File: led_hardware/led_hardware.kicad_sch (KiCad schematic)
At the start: 4 parts, among them Q2 BSS138, U1 STM32F303K8T6

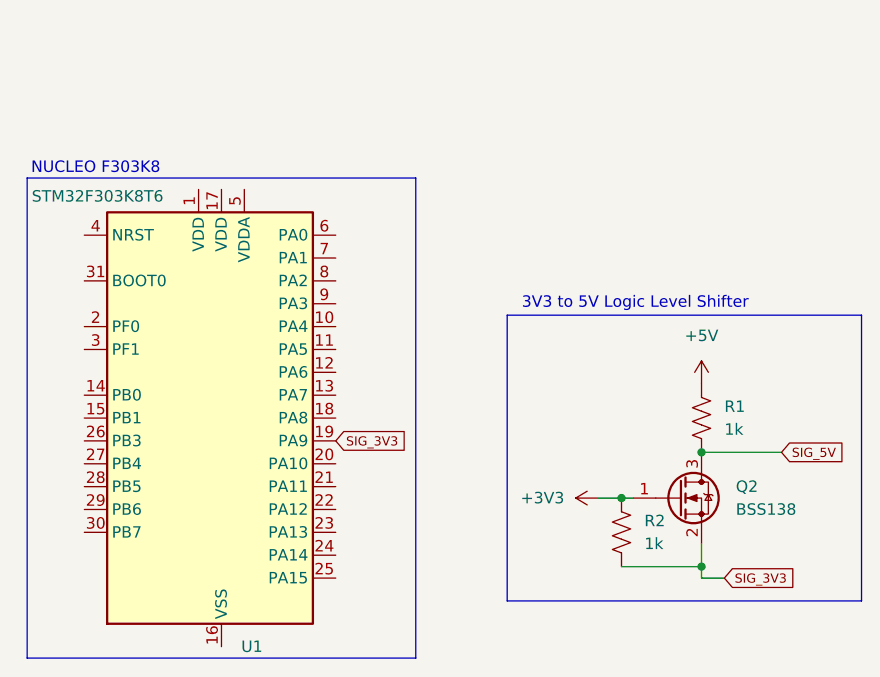
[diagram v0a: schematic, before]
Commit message: used internal timer interrupt to allow for blinking
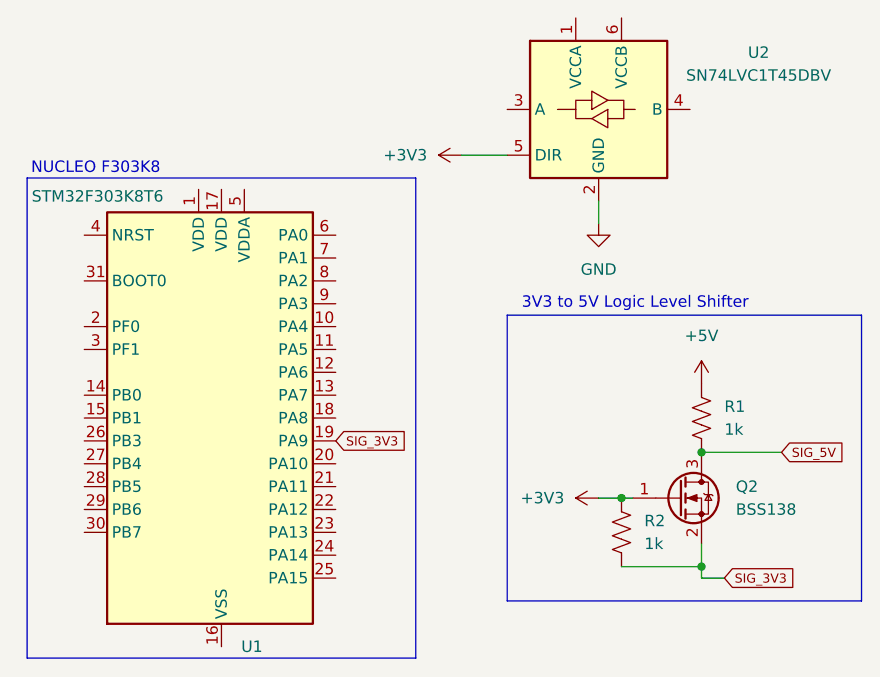
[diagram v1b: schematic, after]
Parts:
- added U2: SN74LVC1T45DBV, Package_TO_SOT_SMD:SOT-23-6, symbol Logic_LevelTranslator:SN74LVC1T45DBV
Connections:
- net +3V3: now also U2.5 (DIR)
- new net GND: U2.2 (GND)
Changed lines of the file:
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@@
+	(wire
+		(pts
+			(xy 151.13 63.5) (xy 151.13 66.04)
+		)
+		(stroke
+			(width 0)
+			(type default)
+		)
+	)
 	(wire
 		(pts
@@
 		(pts
 			(xy 162.56 101.6) (xy 162.56 104.14)
+		)
+		(stroke
+			(width 0)
+			(type default)
+		)
+	)
+	(wire
+		(pts
+			(xy 135.89 58.42) (xy 140.97 58.42)
 		)
 		(stroke
@@
 	)
 	(symbol
+		(lib_id "power:+3V3")
+		(at 135.89 58.42 90)
+		(unit 1)
+		(exclude_from_sim no)
+		(in_bom yes)
+		(on_board yes)
+		(dnp no)
+		(fields_autoplaced yes)
+		(property "Reference" "#PWR03"
+			(at 139.7 58.42 0)
+			(effects
+				(font
+					(size 1.27 1.27)
+				)
+				(hide yes)
+			)
+		)
+		(property "Value" "+3V3"
+			(at 132.08 58.4199 90)
+			(effects
+				(font
+					(size 1.27 1.27)
+				)
+				(justify left)
+			)
+		)
+		(property "Footprint" ""
+			(at 135.89 58.42 0)
+			(effects
+				(font
+					(size 1.27 1.27)
+				)
+				(hide yes)
+			)
+		)
+		(property "Datasheet" ""
+			(at 135.89 58.42 0)
+			(effects
+				(font
+					(size 1.27 1.27)
+				)
+				(hide yes)
+			)
+		)
+		(property "Description" "Power symbol creates a global label with name \"+3V3\""
+			(at 135.89 58.42 0)
+			(effects
+				(font
+					(size 1.27 1.27)
+				)
+				(hide yes)
+			)
+		)
+		(pin "1"
+		)
+		(instances
+			(project ""
+				(path "/0d1e0f9d-c717-4778-96fb-b26f89a362ee"
+					(reference "#PWR03")
+					(unit 1)
+				)
+			)
+		)
+	)
+	(symbol
+		(lib_id "Logic_LevelTranslator:SN74LVC1T45DBV")
+		(at 151.13 53.34 0)
+		(unit 1)
+		(exclude_from_sim no)
+		(in_bom yes)
+		(on_board yes)
+		(dnp no)
+		(fields_autoplaced yes)
+		(property "Reference" "U2"
+			(at 168.91 47.0214 0)
+			(effects
+				(font
+					(size 1.27 1.27)
+				)
+			)
+		)
+		(property "Value" "SN74LVC1T45DBV"
+			(at 168.91 49.5614 0)
+			(effects
+				(font
+					(size 1.27 1.27)
+				)
+			)
+		)
+		(property "Footprint" "Package_TO_SOT_SMD:SOT-23-6"
+			(at 151.13 64.77 0)
+			(effects
+				(font
+					(size 1.27 1.27)
+				)
+				(hide yes)
+			)
+		)
+		(property "Datasheet" "http://www.ti.com/lit/ds/symlink/sn74lvc1t45.pdf"
+			(at 128.27 69.85 0)
+			(effects
+				(font
+					(size 1.27 1.27)
+				)
+				(hide yes)
+			)
+		)
+		(property "Description" "Single-Bit Dual-Supply Bus Transceiver With Configurable Voltage Translation and 3-State Outputs, SOT-23-6"
+			(at 151.13 53.34 0)
+			(effects
+				(font
+					(size 1.27 1.27)
+				)
+				(hide yes)
+			)
+		)
+		(pin "1"
+		)
+		(pin "4"
+		)
+		(pin "3"
+		)
+		(pin "2"
+		)
+		(pin "6"
+		)
+		(pin "5"
+		)
+		(instances
+			(project ""
+				(path "/0d1e0f9d-c717-4778-96fb-b26f89a362ee"
+					(reference "U2")
+					(unit 1)
+				)
+			)
+		)
+	)
+	(symbol
 		(lib_id "Device:R_US")
 		(at 162.56 87.63 0)
@@
 					(unit 1)
 				)
+			)
+		)
+	)
+	(symbol
+		(lib_id "power:GND")
+		(at 151.13 66.04 0)
+		(unit 1)
+		(exclude_from_sim no)
+		(in_bom yes)
+		(on_board yes)
+		(dnp no)
+		(fields_autoplaced yes)
+		(property "Reference" "#PWR04"
+			(at 151.13 72.39 0)
+			(effects
+				(font
+					(size 1.27 1.27)
+				)
+				(hide yes)
+			)
+		)
+		(property "Value" "GND"
+			(at 151.13 71.12 0)
+			(effects
+				(font
+					(size 1.27 1.27)
+				)
+			)
+		)
+		(property "Footprint" ""
+			(at 151.13 66.04 0)
+			(effects
+				(font
+					(size 1.27 1.27)
+				)
+				(hide yes)
+			)
+		)
+		(property "Datasheet" ""
+			(at 151.13 66.04 0)
+			(effects
+				(font
+					(size 1.27 1.27)
+				)
+				(hide yes)
+			)
+		)
+		(property "Description" "Power symbol creates a global label with name \"GND\" , ground"
+			(at 151.13 66.04 0)
+			(effects
+				(font
+					(size 1.27 1.27)
+				)
+				(hide yes)
+			)
+		)
+		(pin "1"
+		)
+		(instances
+			(project ""
+				(path "/0d1e0f9d-c717-4778-96fb-b26f89a362ee"
+					(reference "#PWR04")
+					(unit 1)
+				)
